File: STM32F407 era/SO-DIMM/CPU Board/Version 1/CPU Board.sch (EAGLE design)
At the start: 28 parts, among them U2 TPS3825-33DBVR, Y1 24 MHz, Y2 32.768KHz

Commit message: Started work on new COM-TC module
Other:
- note added: "SO-DIMM Header"
- moved on the sheet: BAT1, C1, C10, C11, C12, C13, C14, C15, C19, C2, C20, C3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

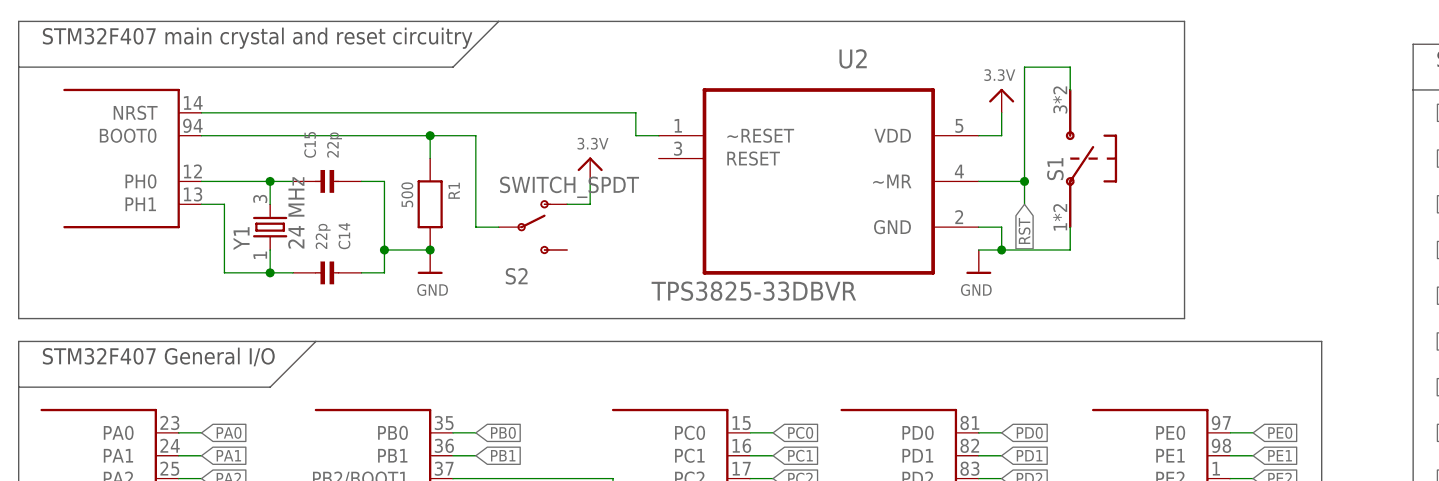
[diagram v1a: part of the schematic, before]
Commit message: USB to UART done, mork work on COM/TC
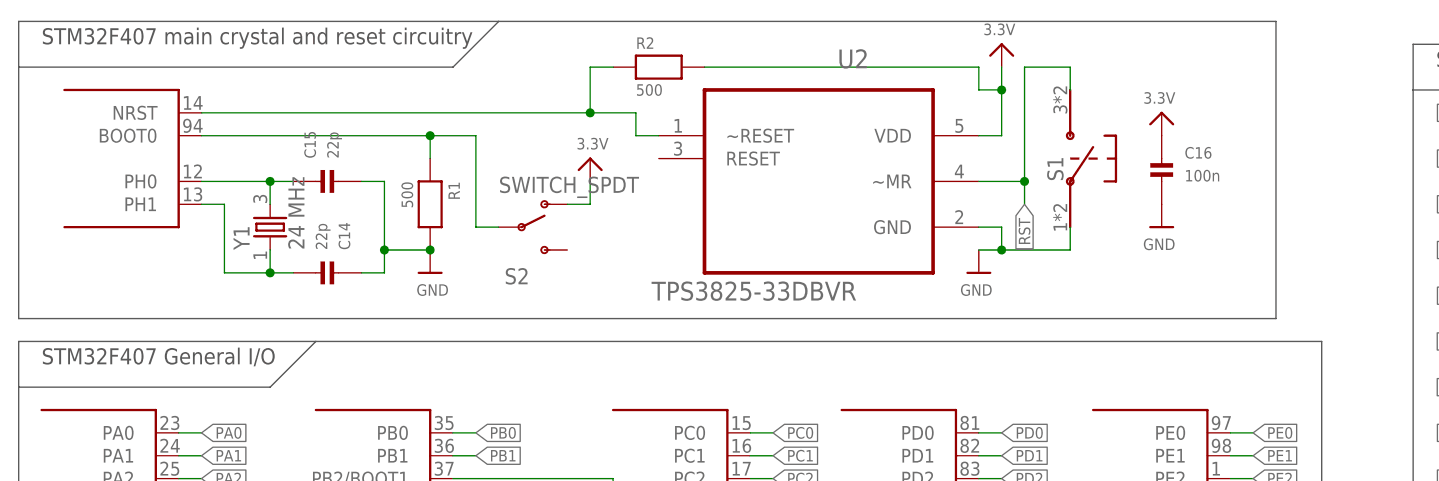
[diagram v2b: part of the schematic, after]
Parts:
- added C16: 100n, microbuilder:CAP_CERAMIC_0603
- added R2: 500, microbuilder:RESISTOR_0603
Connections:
- net 3.3V: now also C16.P$1, R2.2
- net GND: now also C16.P$2
- net RESET: now also R2.1
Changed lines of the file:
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@@
 <part name="U$16" library="microbuilder" deviceset="GND" device=""/>
 <part name="FRAME1" library="SparkFun-Aesthetics" deviceset="FRAME-A4L" device=""/>
+<part name="C16" library="microbuilder" deviceset="CAP_CERAMIC" device="_0603" value="100n"/>
+<part name="U$5" library="microbuilder" deviceset="GND" device=""/>
+<part name="U$17" library="microbuilder" deviceset="3.3V" device=""/>
+<part name="R2" library="microbuilder" deviceset="RESISTOR" device="_0603" value="500"/>
 </parts>
 <sheets>
@@
 <wire x1="35.56" y1="142.24" x2="147.32" y2="142.24" width="0.1524" layer="97"/>
 <wire x1="2.54" y1="177.8" x2="55.88" y2="177.8" width="0.1524" layer="97"/>
-<wire x1="55.88" y1="177.8" x2="132.08" y2="177.8" width="0.1524" layer="97"/>
-<wire x1="132.08" y1="177.8" x2="132.08" y2="144.78" width="0.1524" layer="97"/>
-<wire x1="132.08" y1="144.78" x2="2.54" y2="144.78" width="0.1524" layer="97"/>
+<wire x1="55.88" y1="177.8" x2="142.24" y2="177.8" width="0.1524" layer="97"/>
+<wire x1="142.24" y1="177.8" x2="142.24" y2="144.78" width="0.1524" layer="97"/>
+<wire x1="142.24" y1="144.78" x2="2.54" y2="144.78" width="0.1524" layer="97"/>
 <wire x1="2.54" y1="144.78" x2="2.54" y2="172.72" width="0.1524" layer="97"/>
 <wire x1="2.54" y1="172.72" x2="2.54" y2="177.8" width="0.1524" layer="97"/>
@@
 <instance part="U2" gate="A" x="91.44" y="162.56" rot="MR0"/>
 <instance part="S1" gate="G$1" x="119.38" y="162.56" rot="MR90"/>
-<instance part="U$9" gate="G$1" x="111.76" y="170.18" rot="MR0"/>
+<instance part="U$9" gate="G$1" x="111.76" y="175.26" rot="MR0"/>
 <instance part="U$21" gate="G$1" x="109.22" y="149.86" rot="MR0"/>
 <instance part="U$13" gate="G$1" x="149.86" y="63.5"/>
@@
 <instance part="U$16" gate="G$1" x="251.46" y="38.1"/>
 <instance part="FRAME1" gate="G$1" x="0" y="0"/>
+<instance part="C16" gate="G$1" x="129.54" y="160.02"/>
+<instance part="U$5" gate="G$1" x="129.54" y="154.94" rot="MR0"/>
+<instance part="U$17" gate="G$1" x="129.54" y="167.64" rot="MR0"/>
+<instance part="R2" gate="G$1" x="73.66" y="172.72"/>
 </instances>
 <busses>
@@
 <pinref part="U$16" gate="G$1" pin="GND"/>
 </segment>
+<segment>
+<pinref part="C16" gate="G$1" pin="P$2"/>
+<pinref part="U$5" gate="G$1" pin="GND"/>
+</segment>
 </net>
 <net name="3.3V" class="0">
@@
 <pinref part="U$9" gate="G$1" pin="3.3V"/>
 <wire x1="109.22" y1="165.1" x2="111.76" y2="165.1" width="0.1524" layer="91"/>
-<wire x1="111.76" y1="165.1" x2="111.76" y2="167.64" width="0.1524" layer="91"/>
+<wire x1="111.76" y1="165.1" x2="111.76" y2="170.18" width="0.1524" layer="91"/>
+<pinref part="R2" gate="G$1" pin="2"/>
+<wire x1="111.76" y1="170.18" x2="111.76" y2="172.72" width="0.1524" layer="91"/>
+<wire x1="78.74" y1="172.72" x2="109.22" y2="172.72" width="0.1524" layer="91"/>
+<wire x1="109.22" y1="172.72" x2="109.22" y2="170.18" width="0.1524" layer="91"/>
+<wire x1="109.22" y1="170.18" x2="111.76" y2="170.18" width="0.1524" layer="91"/>
+<junction x="111.76" y="170.18"/>
 </segment>
 <segment>
@@
 <wire x1="147.32" y1="50.8" x2="147.32" y2="58.42" width="0.1524" layer="91"/>
 <junction x="147.32" y="58.42"/>
+</segment>
+<segment>
+<pinref part="C16" gate="G$1" pin="P$1"/>
+<pinref part="U$17" gate="G$1" pin="3.3V"/>
 </segment>
 </net>
@@
 <segment>
 <pinref part="U1" gate="G$7" pin="NRST"/>
-<wire x1="22.86" y1="167.64" x2="71.12" y2="167.64" width="0.1524" layer="91"/>
+<wire x1="22.86" y1="167.64" x2="66.04" y2="167.64" width="0.1524" layer="91"/>
+<wire x1="66.04" y1="167.64" x2="71.12" y2="167.64" width="0.1524" layer="91"/>
 <wire x1="71.12" y1="167.64" x2="71.12" y2="165.1" width="0.1524" layer="91"/>
 <pinref part="U2" gate="A" pin="~RESET"/>
 <wire x1="71.12" y1="165.1" x2="73.66" y2="165.1" width="0.1524" layer="91"/>
-</segment>
-</net>
+<pinref part="R2" gate="G$1" pin="1"/>
+<wire x1="68.58" y1="172.72" x2="66.04" y2="172.72" width="0.1524" layer="91"/>
+<wire x1="66.04" y1="172.72" x2="66.04" y2="167.64" width="0.1524" layer="91"/>
+<junction x="66.04" y="167.64"/>
+</segment>
+</net>
